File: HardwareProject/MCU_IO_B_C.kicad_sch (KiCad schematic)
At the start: 3 parts, among them U4 HPM6P41IPB1

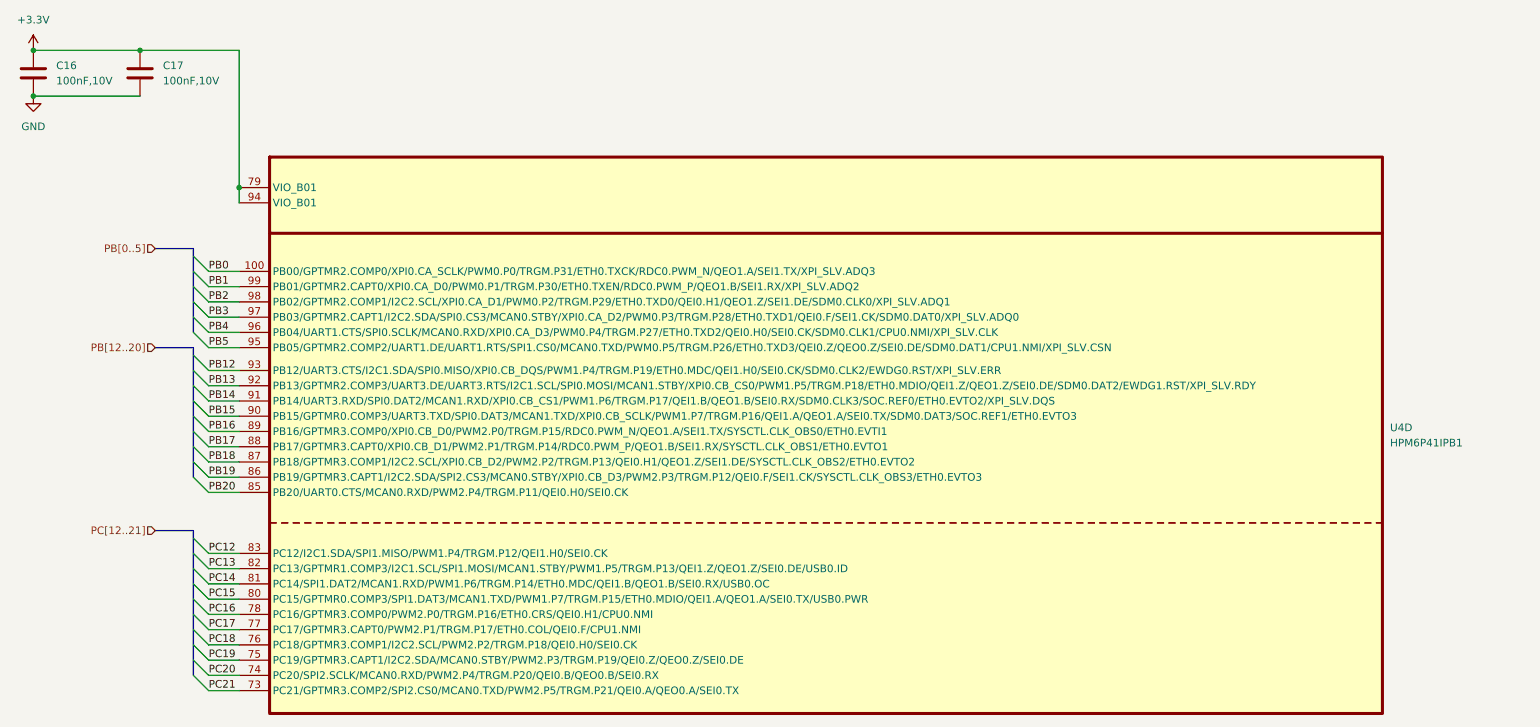
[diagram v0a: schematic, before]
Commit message: rev4修改核心供电前保存（当前SYR838）
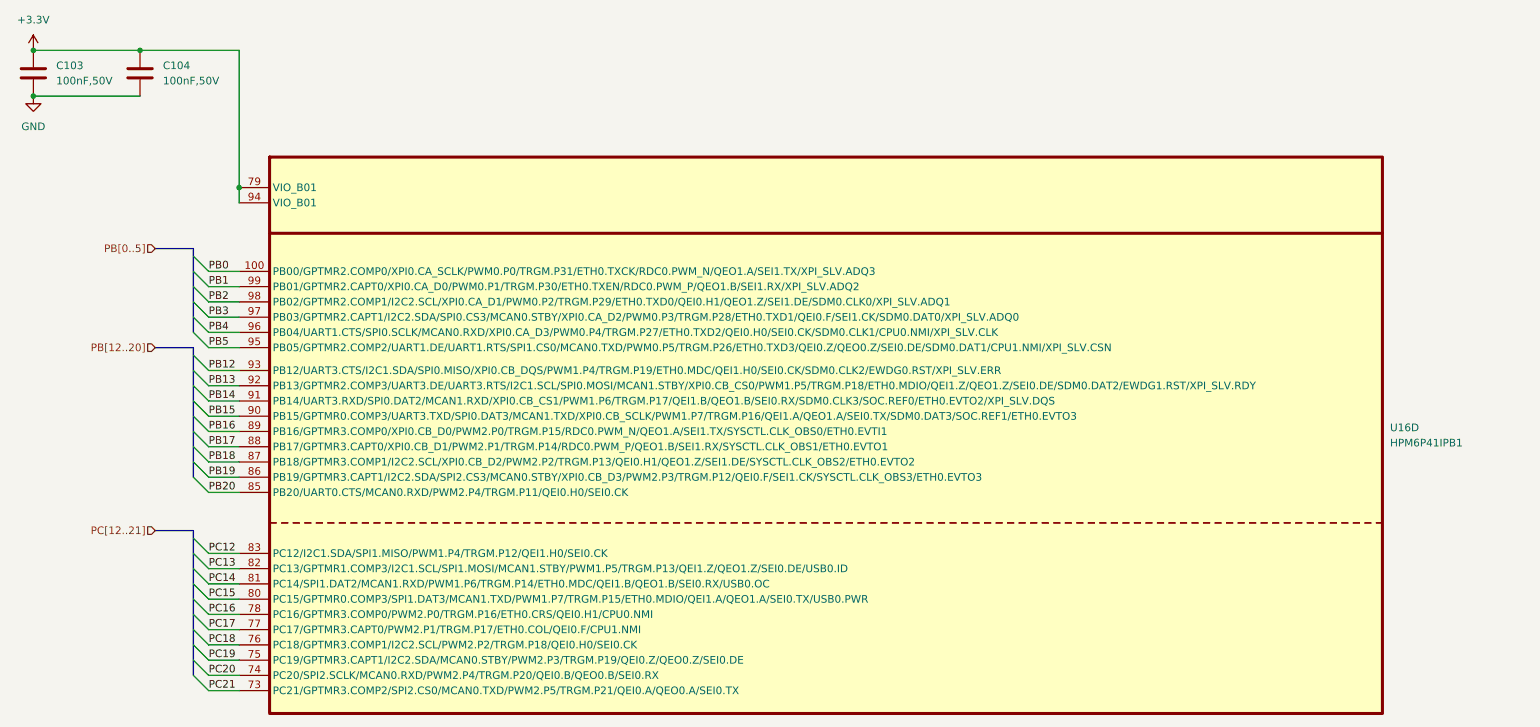
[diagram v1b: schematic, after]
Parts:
- C103: renamed from C16; value 100nF,10V -> 100nF,50V
- C104: renamed from C17; value 100nF,10V -> 100nF,50V
- renumbered U4 to U16
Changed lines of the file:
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@@
 		(on_board yes)
 		(dnp no)
-		(property "Reference" "C17"
+		(property "Reference" "C104"
 			(at 62.23 29.2099 0)
 			(effects
@@
 			)
 		)
-		(property "Value" "100nF,10V"
+		(property "Value" "100nF,50V"
 			(at 62.23 31.7499 0)
 			(effects
@@
 			(project "HPM6P41_BB"
 				(path "/714b8a30-f9a7-49d4-a000-bc20c4884c7a/0f167a17-4597-4a00-9bee-6bca96cc31c3"
-					(reference "C17")
+					(reference "C104")
 					(unit 1)
 				)
@@
 		(dnp no)
 		(fields_autoplaced yes)
-		(property "Reference" "#PWR033"
+		(property "Reference" "#PWR0194"
 			(at 40.64 30.48 0)
 			(effects
@@
 			(project "HPM6P41_BB"
 				(path "/714b8a30-f9a7-49d4-a000-bc20c4884c7a/0f167a17-4597-4a00-9bee-6bca96cc31c3"
-					(reference "#PWR033")
+					(reference "#PWR0194")
 					(unit 1)
 				)
@@
 		(dnp no)
 		(fields_autoplaced yes)
-		(property "Reference" "U4"
+		(property "Reference" "U16"
 			(at 266.7 89.5349 0)
 			(effects
@@
 			(project "HPM6P41_BB"
 				(path "/714b8a30-f9a7-49d4-a000-bc20c4884c7a/0f167a17-4597-4a00-9bee-6bca96cc31c3"
-					(reference "U4")
+					(reference "U16")
 					(unit 4)
 				)
@@
 		(dnp no)
 		(fields_autoplaced yes)
-		(property "Reference" "#PWR034"
+		(property "Reference" "#PWR0195"
 			(at 40.64 40.64 0)
 			(effects
@@
 			(project "HPM6P41_BB"
 				(path "/714b8a30-f9a7-49d4-a000-bc20c4884c7a/0f167a17-4597-4a00-9bee-6bca96cc31c3"
-					(reference "#PWR034")
+					(reference "#PWR0195")
 					(unit 1)
 				)
@@
 		(on_board yes)
 		(dnp no)
-		(property "Reference" "C16"
+		(property "Reference" "C103"
 			(at 44.45 29.2099 0)
 			(effects
@@
 			)
 		)
-		(property "Value" "100nF,10V"
+		(property "Value" "100nF,50V"
 			(at 44.45 31.7499 0)
 			(effects
@@
 			(project "HPM6P41_BB"
 				(path "/714b8a30-f9a7-49d4-a000-bc20c4884c7a/0f167a17-4597-4a00-9bee-6bca96cc31c3"
-					(reference "C16")
+					(reference "C103")
 					(unit 1)
 				)
